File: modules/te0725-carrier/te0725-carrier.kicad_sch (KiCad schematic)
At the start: 0 parts

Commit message: add wider footprint for TE0725 carrier
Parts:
- added J1, J2: Conn_02x25_Odd_Even, Connector_PinHeader_2.54mm:PinHeader_2x25_P2.54mm_Vertical, symbol Connector_Generic:Conn_02x25_Odd_Even
- added M1: ~, MegaCastle:MegaCastle2x52-Module-I33.6x127.3-M1, symbol MegaCastle:MegaCastle2x52-Module-I33.6x127.3-M1

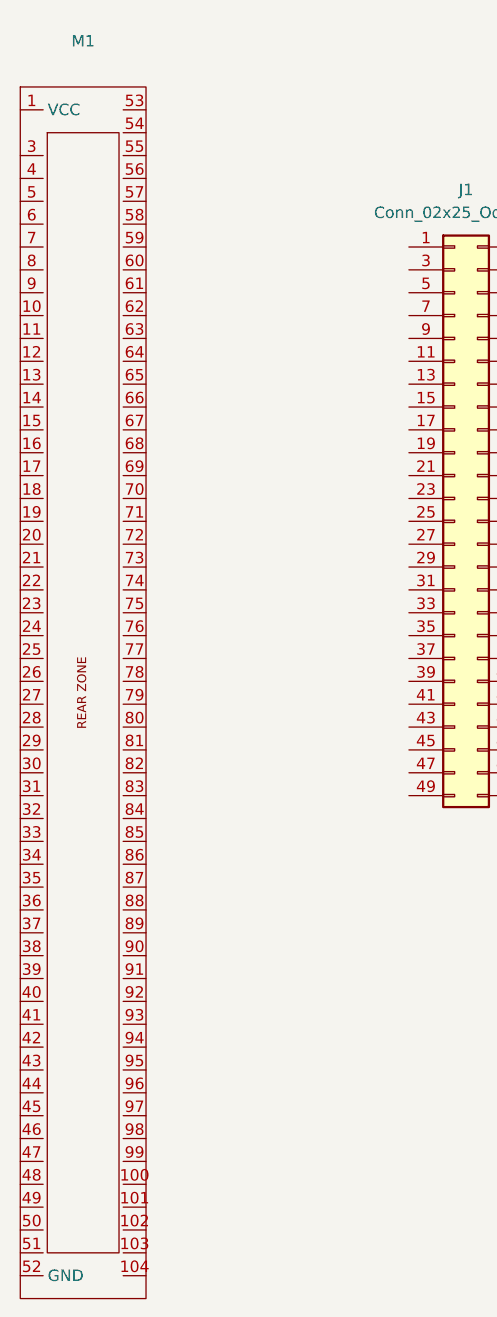
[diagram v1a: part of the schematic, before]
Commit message: and even wider module for TE0725
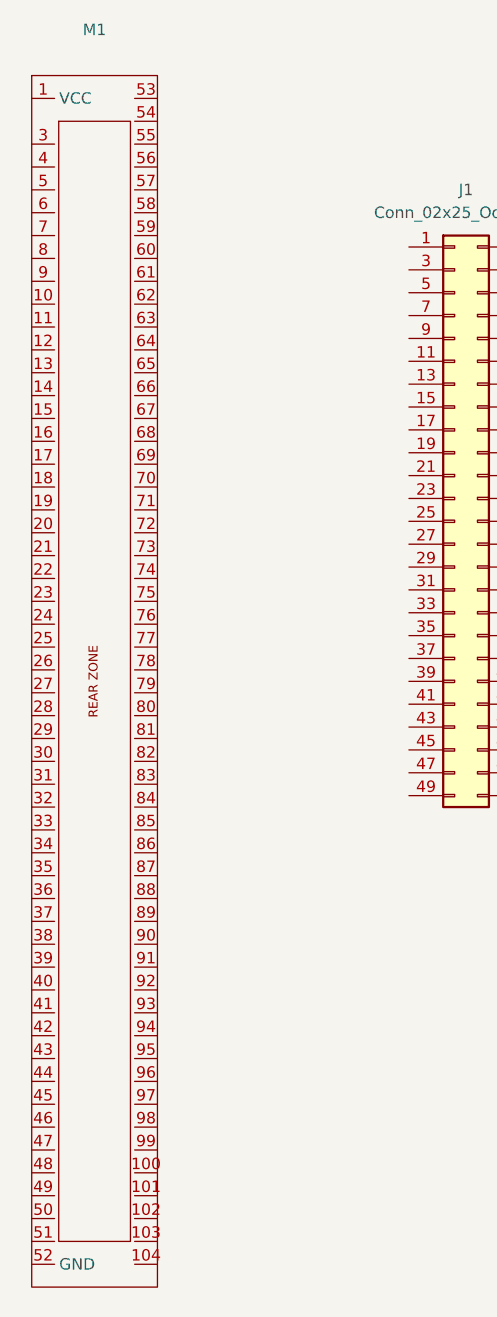
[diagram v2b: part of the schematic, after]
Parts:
- removed M1: ~, MegaCastle:MegaCastle2x52-Module-I33.6x127.3-M1, symbol MegaCastle:MegaCastle2x52-Module-I33.6x127.3-M1
- added M1: ~, MegaCastle:MegaCastle2x52-Module-I37.0x127.3-M1, symbol MegaCastle:MegaCastle2x52-Module-I37.0x127.3-M1
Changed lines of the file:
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@@
 	)
 	(symbol
-		(lib_id "MegaCastle:MegaCastle2x52-Module-I33.6x127.3-M1")
-		(at 46.99 101.6 0)
+		(lib_id "MegaCastle:MegaCastle2x52-Module-I37.0x127.3-M1")
+		(at 48.26 100.33 0)
 		(unit 1)
 		(exclude_from_sim no)
@@
 		(fields_autoplaced yes)
 		(property "Reference" "M1"
-			(at 47.625 29.21 0)
+			(at 48.895 27.94 0)
 			(effects
 				(font
@@
 		)
 		(property "Value" "~"
-			(at 47.625 31.75 0)
-			(effects
-				(font
-					(size 1.27 1.27)
-				)
-			)
-		)
-		(property "Footprint" "MegaCastle:MegaCastle2x52-Module-I33.6x127.3-M1"
-			(at 46.99 173.99 0)
+			(at 48.895 30.48 0)
+			(effects
+				(font
+					(size 1.27 1.27)
+				)
+			)
+		)
+		(property "Footprint" "MegaCastle:MegaCastle2x52-Module-I37.0x127.3-M1"
+			(at 48.26 172.72 0)
 			(effects
 				(font
@@
 		)
 		(property "Datasheet" ""
-			(at 46.99 96.52 0)
+			(at 48.26 95.25 0)
 			(effects
 				(font
@@
 			)
 		)
-		(property "Description" "Generated using footprint-gen . 33.64 72.12 102"
-			(at 46.99 101.6 0)
+		(property "Description" "Generated using footprint-gen . 37 72.12 102"
+			(at 48.26 100.33 0)
 			(effects
 				(font
@@
 			)
 		)
+		(pin "58"
+		)
+		(pin "62"
+		)
+		(pin "46"
+		)
+		(pin "98"
+		)
+		(pin "45"
+		)
+		(pin "56"
+		)
+		(pin "99"
+		)
+		(pin "74"
+		)
+		(pin "12"
+		)
+		(pin "83"
+		)
+		(pin "100"
+		)
+		(pin "92"
+		)
+		(pin "59"
+		)
+		(pin "61"
+		)
+		(pin "18"
+		)
+		(pin "66"
+		)
+		(pin "42"
+		)
+		(pin "64"
+		)
+		(pin "95"
+		)
+		(pin "87"
+		)
+		(pin "43"
+		)
+		(pin "14"
+		)
+		(pin "93"
+		)
+		(pin "94"
+		)
+		(pin "88"
+		)
+		(pin "60"
+		)
+		(pin "85"
+		)
+		(pin "89"
+		)
+		(pin "19"
+		)
+		(pin "49"
+		)
+		(pin "91"
+		)
+		(pin "9"
+		)
+		(pin "68"
+		)
+		(pin "51"
+		)
+		(pin "44"
+		)
+		(pin "50"
+		)
+		(pin "80"
+		)
+		(pin "72"
+		)
+		(pin "73"
+		)
+		(pin "82"
+		)
+		(pin "69"
+		)
+		(pin "55"
+		)
+		(pin "21"
+		)
+		(pin "90"
+		)
+		(pin "96"
+		)
+		(pin "17"
+		)
+		(pin "84"
+		)
+		(pin "53"
+		)
+		(pin "16"
+		)
+		(pin "71"
+		)
+		(pin "13"
+		)
+		(pin "11"
+		)
+		(pin "20"
+		)
+		(pin "57"
+		)
+		(pin "76"
+		)
+		(pin "10"
+		)
+		(pin "75"
+		)
+		(pin "81"
+		)
+		(pin "52"
+		)
+		(pin "70"
+		)
 		(pin "86"
 		)
-		(pin "100"
-		)
-		(pin "99"
-		)
-		(pin "95"
-		)
-		(pin "98"
+		(pin "67"
+		)
+		(pin "41"
+		)
+		(pin "40"
+		)
+		(pin "39"
+		)
+		(pin "38"
+		)
+		(pin "37"
+		)
+		(pin "36"
+		)
+		(pin "79"
+		)
+		(pin "35"
+		)
+		(pin "34"
+		)
+		(pin "78"
+		)
+		(pin "33"
+		)
+		(pin "32"
+		)
+		(pin "31"
+		)
+		(pin "30"
+		)
+		(pin "29"
+		)
+		(pin "28"
+		)
+		(pin "77"
+		)
+		(pin "27"
+		)
+		(pin "26"
+		)
+		(pin "25"
+		)
+		(pin "104"
+		)
+		(pin "103"
+		)
+		(pin "102"
+		)
+		(pin "24"
+		)
+		(pin "23"
+		)
+		(pin "101"
+		)
+		(pin "22"
 		)
 		(pin "6"
 		)
-		(pin "60"
-		)
-		(pin "92"
-		)
-		(pin "88"
+		(pin "5"
+		)
+		(pin "4"
+		)
+		(pin "3"
+		)
+		(pin "1"
+		)
+		(pin "8"
+		)
+		(pin "7"
+		)
+		(pin "15"
+		)
+		(pin "54"
+		)
+		(pin "63"
+		)
+		(pin "47"
+		)
+		(pin "65"
 		)
 		(pin "97"
 		)
-		(pin "85"
-		)
-		(pin "90"
-		)
-		(pin "87"
-		)
-		(pin "73"
-		)
-		(pin "91"
-		)
-		(pin "51"
-		)
-		(pin "45"
-		)
-		(pin "65"
-		)
-		(pin "43"
-		)
-		(pin "67"
-		)
-		(pin "66"
-		)
-		(pin "7"
-		)
-		(pin "93"
-		)
-		(pin "15"
-		)
-		(pin "4"
-		)
-		(pin "5"
-		)
-		(pin "78"
-		)
-		(pin "56"
-		)
-		(pin "13"
-		)
-		(pin "80"
-		)
-		(pin "82"
-		)
-		(pin "54"
-		)
-		(pin "42"
-		)
-		(pin "94"
-		)
-		(pin "83"
-		)
-		(pin "50"
-		)
-		(pin "46"
-		)
-		(pin "103"
-		)
-		(pin "57"
-		)
-		(pin "102"
-		)
-		(pin "89"
-		)
-		(pin "104"
-		)
-		(pin "71"
-		)
 		(pin "48"
 		)
-		(pin "14"
-		)
-		(pin "53"
-		)
-		(pin "74"
-		)
-		(pin "62"
-		)
-		(pin "61"
-		)
-		(pin "101"
-		)
-		(pin "64"
-		)
-		(pin "3"
-		)
-		(pin "1"
-		)
-		(pin "44"
-		)
-		(pin "79"
-		)
-		(pin "58"
-		)
-		(pin "75"
-		)
-		(pin "69"
-		)
-		(pin "55"
-		)
-		(pin "84"
-		)
-		(pin "8"
-		)
-		(pin "70"
-		)
-		(pin "41"
-		)
-		(pin "96"
-		)
-		(pin "72"
-		)
-		(pin "35"
-		)
-		(pin "59"
-		)
-		(pin "47"
-		)
-		(pin "76"
-		)
-		(pin "9"
-		)
-		(pin "63"
-		)
-		(pin "40"
-		)
-		(pin "33"
-		)
-		(pin "11"
-		)
-		(pin "24"
-		)
-		(pin "10"
-		)
-		(pin "25"
-		)
-		(pin "17"
-		)
-		(pin "21"
-		)
-		(pin "31"
-		)
-		(pin "12"
-		)
-		(pin "23"
-		)
-		(pin "30"
-		)
-		(pin "18"
-		)
-		(pin "29"
-		)
-		(pin "28"
-		)
-		(pin "22"
-		)
-		(pin "27"
-		)
-		(pin "20"
-		)
-		(pin "32"
-		)
-		(pin "68"
-		)
-		(pin "52"
-		)
-		(pin "16"
-		)
-		(pin "36"
-		)
-		(pin "38"
-		)
-		(pin "34"
-		)
-		(pin "39"
-		)
-		(pin "37"
-		)
-		(pin "26"
-		)
-		(pin "19"
-		)
-		(pin "77"
-		)
-		(pin "49"
-		)
-		(pin "81"
-		)
 		(instances

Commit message: route etc on TE0725 carrier module
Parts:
- removed M1: ~, MegaCastle:MegaCastle2x52-Module-I37.0x127.3-M1, symbol MegaCastle:MegaCastle2x52-Module-I37.0x127.3-M1
- added M1: ~, MegaCastle:MegaCastle2x52-Module-I42.0x127.3-M1, symbol MegaCastle:MegaCastle2x52-Module-I42.0x127.3-M1
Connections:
- net GND: now reaches J1.1 (Pin_1)
- net GND: now also J1.2 (Pin_2), J1.49 (Pin_49), J1.50 (Pin_50), J2.1 (Pin_1), J2.2 (Pin_2), J2.49 (Pin_49), J2.50 (Pin_50), M1.104, M1.27, M1.28, M1.3, M1.52 (GND), M1.55, M1.79, M1.80
- net J1_10: now reaches J1.10 (Pin_10)
- net J1_10: now also M1.48
- net J1_11: now reaches J1.11 (Pin_11)
- net J1_11: now also M1.8
- net J1_12: now reaches J1.12 (Pin_12)
- net J1_12: now also M1.47
- net J1_13: now reaches J1.13 (Pin_13)
- net J1_13: now also M1.9
- net J1_14: now reaches J1.14 (Pin_14)
- net J1_14: now also M1.46
- net J1_15: now reaches J1.15 (Pin_15)
- net J1_15: now also M1.10
- net J1_16: now reaches J1.16 (Pin_16)
- net J1_16: now also M1.45
- net J1_17: now reaches J1.17 (Pin_17)
- net J1_17: now also M1.11
- net J1_18: now reaches J1.18 (Pin_18)
- net J1_18: now also M1.44
- net J1_19: now reaches J1.19 (Pin_19)
- net J1_19: now also M1.12
- net J1_20: now reaches J1.20 (Pin_20)
- net J1_20: now also M1.43
- net J1_21: now reaches J1.21 (Pin_21)
- net J1_21: now also M1.13
- net J1_22: now reaches J1.22 (Pin_22)
- net J1_22: now also M1.42
- net J1_23: now reaches J1.23 (Pin_23)
- net J1_23: now also M1.14
- net J1_24: now reaches J1.24 (Pin_24)
- net J1_24: now also M1.41
- net J1_25: now reaches J1.25 (Pin_25)
- net J1_25: now also M1.15
- net J1_26: now reaches J1.26 (Pin_26)
- net J1_26: now also M1.40
- net J1_27: now reaches J1.27 (Pin_27)
- net J1_27: now also M1.16
- net J1_28: now reaches J1.28 (Pin_28)
- net J1_28: now also M1.39
- net J1_29: now reaches J1.29 (Pin_29)
- net J1_29: now also M1.17
- net J1_3: now reaches J1.3 (Pin_3)
- net J1_3: now also M1.4
- net J1_30: now reaches J1.30 (Pin_30)
- net J1_30: now also M1.38
- net J1_31: now reaches J1.31 (Pin_31)
- net J1_31: now also M1.18
- net J1_32: now reaches J1.32 (Pin_32)
- net J1_32: now also M1.37
- net J1_33: now reaches J1.33 (Pin_33)
- net J1_33: now also M1.19
- net J1_34: now reaches J1.34 (Pin_34)
- net J1_34: now also M1.36
- net J1_35: now reaches J1.35 (Pin_35)
- net J1_35: now also M1.20
- net J1_36: now reaches J1.36 (Pin_36)
- net J1_36: now also M1.35
- net J1_37: now reaches J1.37 (Pin_37)
- net J1_37: now also M1.21
- net J1_38: now reaches J1.38 (Pin_38)
- net J1_38: now also M1.34
- net J1_39: now reaches J1.39 (Pin_39)
- net J1_39: now also M1.22
- net J1_4: now reaches J1.4 (Pin_4)
- net J1_4: now also M1.51
- net J1_40: now reaches J1.40 (Pin_40)
- net J1_40: now also M1.33
- net J1_41: now reaches J1.41 (Pin_41)
- net J1_41: now also M1.23
- net J1_42: now reaches J1.42 (Pin_42)
- net J1_42: now also M1.32
- net J1_43: now reaches J1.43 (Pin_43)
- net J1_43: now also M1.24
- net J1_44: now reaches J1.44 (Pin_44)
- net J1_44: now also M1.31
- net VCCIO: now reaches J1.45 (Pin_45)
- net VCCIO: now also J1.6 (Pin_6), J2.45 (Pin_45), J2.6 (Pin_6), M1.102, M1.25, M1.50, M1.53, M1.77
- net +3.3V: now reaches J1.46 (Pin_46)
- net +3.3V: now also J1.5 (Pin_5), J2.46 (Pin_46), J2.5 (Pin_5), M1.1 (VCC), M1.30, M1.5, M1.57, M1.82
- net J1_47: now reaches J1.47 (Pin_47)
- net J1_47: now also M1.26
- net J1_48: now reaches J1.48 (Pin_48)
- net J1_48: now also M1.29
- net J1_7: now reaches J1.7 (Pin_7)
- net J1_7: now also M1.6
- net J1_8: now reaches J1.8 (Pin_8)
- net J1_8: now also M1.49
- net J1_9: now reaches J1.9 (Pin_9)
- net J1_9: now also M1.7
- net J2_10: now reaches J2.10 (Pin_10)
- net J2_10: now also M1.100
- net J2_11: now reaches J2.11 (Pin_11)
- net J2_11: now also M1.60
- net J2_12: now reaches J2.12 (Pin_12)
- net J2_12: now also M1.99
- net J2_13: now reaches J2.13 (Pin_13)
- net J2_13: now also M1.61
- net J2_14: now reaches J2.14 (Pin_14)
- net J2_14: now also M1.98
- net J2_15: now reaches J2.15 (Pin_15)
- net J2_15: now also M1.62
- net J2_16: now reaches J2.16 (Pin_16)
- net J2_16: now also M1.97
- net J2_17: now reaches J2.17 (Pin_17)
- net J2_17: now also M1.63
- net J2_18: now reaches J2.18 (Pin_18)
- net J2_18: now also M1.96
- net J2_19: now reaches J2.19 (Pin_19)
- net J2_19: now also M1.64
- net J2_20: now reaches J2.20 (Pin_20)
- net J2_20: now also M1.95
- net J2_21: now reaches J2.21 (Pin_21)
- net J2_21: now also M1.65
- net J2_22: now reaches J2.22 (Pin_22)
- net J2_22: now also M1.94
- net J2_23: now reaches J2.23 (Pin_23)
- net J2_23: now also M1.66
- net J2_24: now reaches J2.24 (Pin_24)
- net J2_24: now also M1.93
- net J2_25: now reaches J2.25 (Pin_25)
- net J2_25: now also M1.67
- net J2_26: now reaches J2.26 (Pin_26)
- net J2_26: now also M1.92
- net J2_27: now reaches J2.27 (Pin_27)
- net J2_27: now also M1.68
- net J2_28: now reaches J2.28 (Pin_28)
- net J2_28: now also M1.91
- net J2_29: now reaches J2.29 (Pin_29)
- net J2_29: now also M1.69
- net J2_3: now reaches J2.3 (Pin_3)
- net J2_3: now also M1.56
- net J2_30: now reaches J2.30 (Pin_30)
- net J2_30: now also M1.90
- net J2_31: now reaches J2.31 (Pin_31)
- net J2_31: now also M1.70
- net J2_32: now reaches J2.32 (Pin_32)
- net J2_32: now also M1.89
- net J2_33: now reaches J2.33 (Pin_33)
- net J2_33: now also M1.71
- net J2_34: now reaches J2.34 (Pin_34)
- net J2_34: now also M1.88
- net J2_35: now reaches J2.35 (Pin_35)
- net J2_35: now also M1.72
- net J2_36: now reaches J2.36 (Pin_36)
- net J2_36: now also M1.87
- net J2_37: now reaches J2.37 (Pin_37)
- net J2_37: now also M1.73
- net J2_38: now reaches J2.38 (Pin_38)
- net J2_38: now also M1.86
- net J2_39: now reaches J2.39 (Pin_39)
- net J2_39: now also M1.74
- net J2_4: now reaches J2.4 (Pin_4)
- net J2_4: now also M1.103
- net J2_40: now reaches J2.40 (Pin_40)
- net J2_40: now also M1.85
- net J2_41: now reaches J2.41 (Pin_41)
- net J2_41: now also M1.75
- net J2_42: now reaches J2.42 (Pin_42)
- net J2_42: now also M1.84
- net J2_43: now reaches J2.43 (Pin_43)
- net J2_43: now also M1.76
- net J2_44: now reaches J2.44 (Pin_44)
- net J2_44: now also M1.83
- net J2_47: now reaches J2.47 (Pin_47)
- net J2_47: now also M1.78
- net J2_48: now reaches J2.48 (Pin_48)
- net J2_48: now also M1.81
- net J2_7: now reaches J2.7 (Pin_7)
- net J2_7: now also M1.58
- net J2_8: now reaches J2.8 (Pin_8)
- net J2_8: now also M1.101
- net J2_9: now reaches J2.9 (Pin_9)
- net J2_9: now also M1.59
- no-connect marks 0 -> 1
